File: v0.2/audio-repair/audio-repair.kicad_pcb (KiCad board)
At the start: 2 copper layers, 50 x 50 mm, 28 parts, among them J2 Switchcraft_35RAPC4BHN3, J3 PL, J5 UVP, U1 PAM8019KGR, U2 1bitsy-basic-stubby

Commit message: Add mounting holes; tweak stuff.
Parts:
- added REF**: MountingHole_2.2mm_M2_Pad_Via, audio-repair:MountingHole_2.2mm_M2_Pad_Via, F.Cu at (103.5, 103.5)
- added REF**: MountingHole_2.2mm_M2_Pad_Via, audio-repair:MountingHole_2.2mm_M2_Pad_Via, F.Cu at (103.5, 146.5)
- added REF**: MountingHole_2.2mm_M2_Pad_Via, audio-repair:MountingHole_2.2mm_M2_Pad_Via, F.Cu at (146.5, 146.5)
- added REF**: MountingHole_2.2mm_M2_Pad_Via, audio-repair:MountingHole_2.2mm_M2_Pad_Via, F.Cu at (146.5, 103.5)
- moved Left 5.50 mm to (148.0, 138.5)
- moved Right 5.50 mm to (148.0, 129.5)
- moved 3v3 Pwr 5.39 mm to (113.0, 141.0)
- moved C1 5.39 mm to (113.0, 146.0)
- moved Pwr 5.39 mm to (108.8, 144.8)
- moved C2 0.30 mm to (126.3, 120.4)
- moved C3 0.30 mm to (123.7, 120.4)
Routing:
- net VDD: track 127.4 -> 120.0 mm
- net Net-(J4-Pad1): track 59.9 -> 54.5 mm
- net Net-(J6-Pad2): track 43.6 -> 38.8 mm
- net Net-(J6-Pad1): track 43.0 -> 38.4 mm
- net Net-(J4-Pad2): track 44.5 -> 40.7 mm
- net +3V3: track 53.8 -> 57.1 mm
- net Net-(J3-Pad2): track 37.0 -> 38.9 mm
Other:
- outline, holes or cut-outs redrawn
- net class Power added: clearance 0.1524, trace_width 0.3, via_dia 0.6858, via_drill 0.3302
- net class Speaker added: clearance 0.1524, trace_width 0.3, via_dia 0.6858, via_drill 0.3302

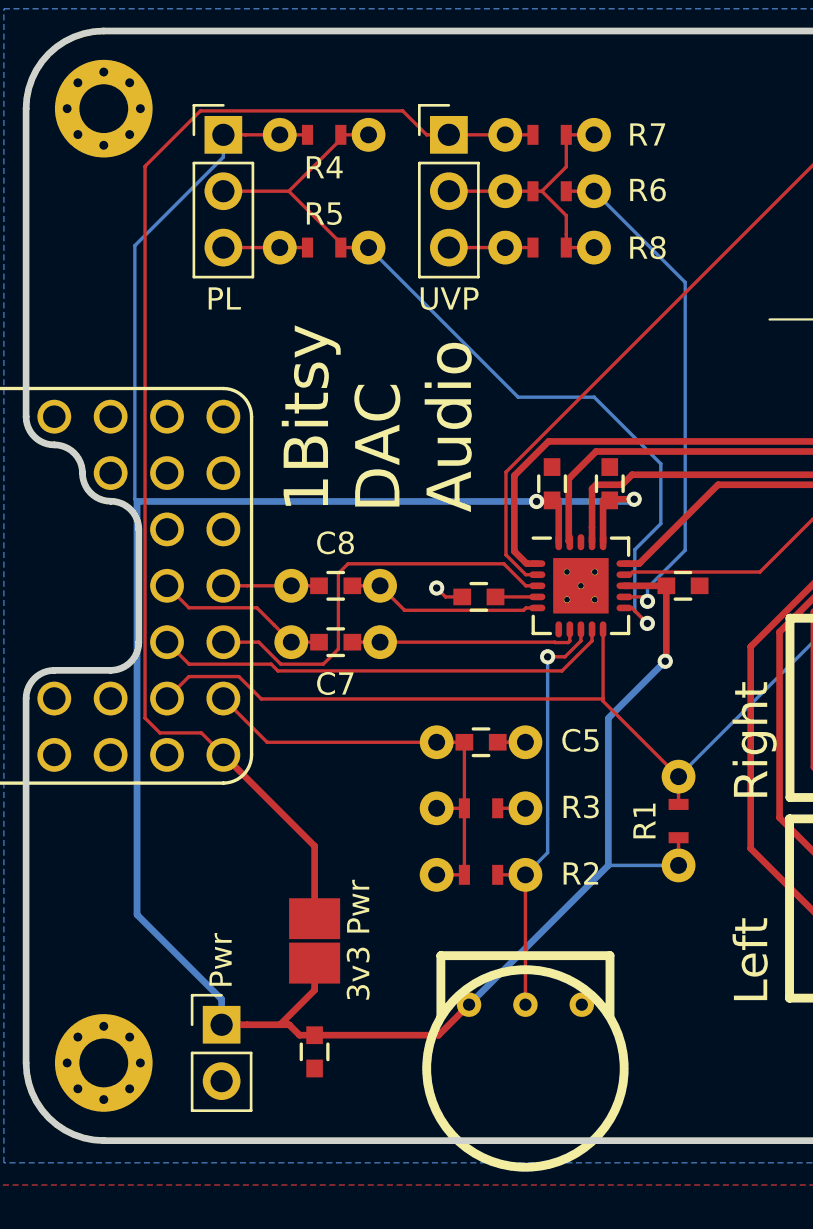
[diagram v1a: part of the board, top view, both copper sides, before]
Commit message: Change 3.3v jumper from solder jumper to pin header.
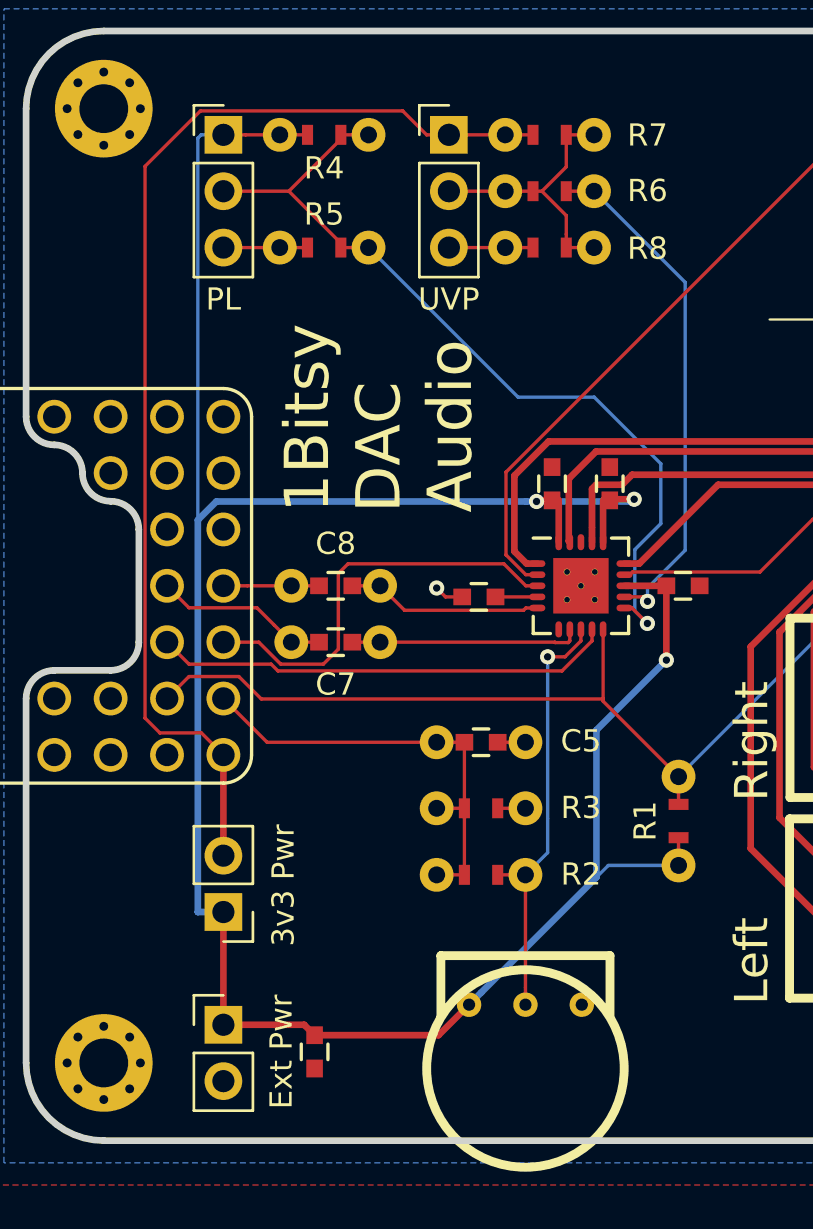
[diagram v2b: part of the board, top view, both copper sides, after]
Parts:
- removed the 3v3 Pwr at (113.0, 141.0)
- added 3v3 Pwr: Jumper, Pin_Headers:Pin_Header_Straight_1x02_Pitch2.54mm, F.Cu at (108.9, 139.7)
- Ext Pwr: renamed from Pwr
- moved Ext Pwr 0.08 mm to (108.9, 144.8)
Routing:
- net VDD: track 120.0 -> 113.8 mm
- net +3V3: track 57.1 -> 52.6 mm
